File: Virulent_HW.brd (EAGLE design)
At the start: 58.2 x 43 mm, 96 parts, among them SW1 COM08229, SW2 COM08720, SW3 BUTTON, U1 STM32F050G6U6, U2 MAX14536

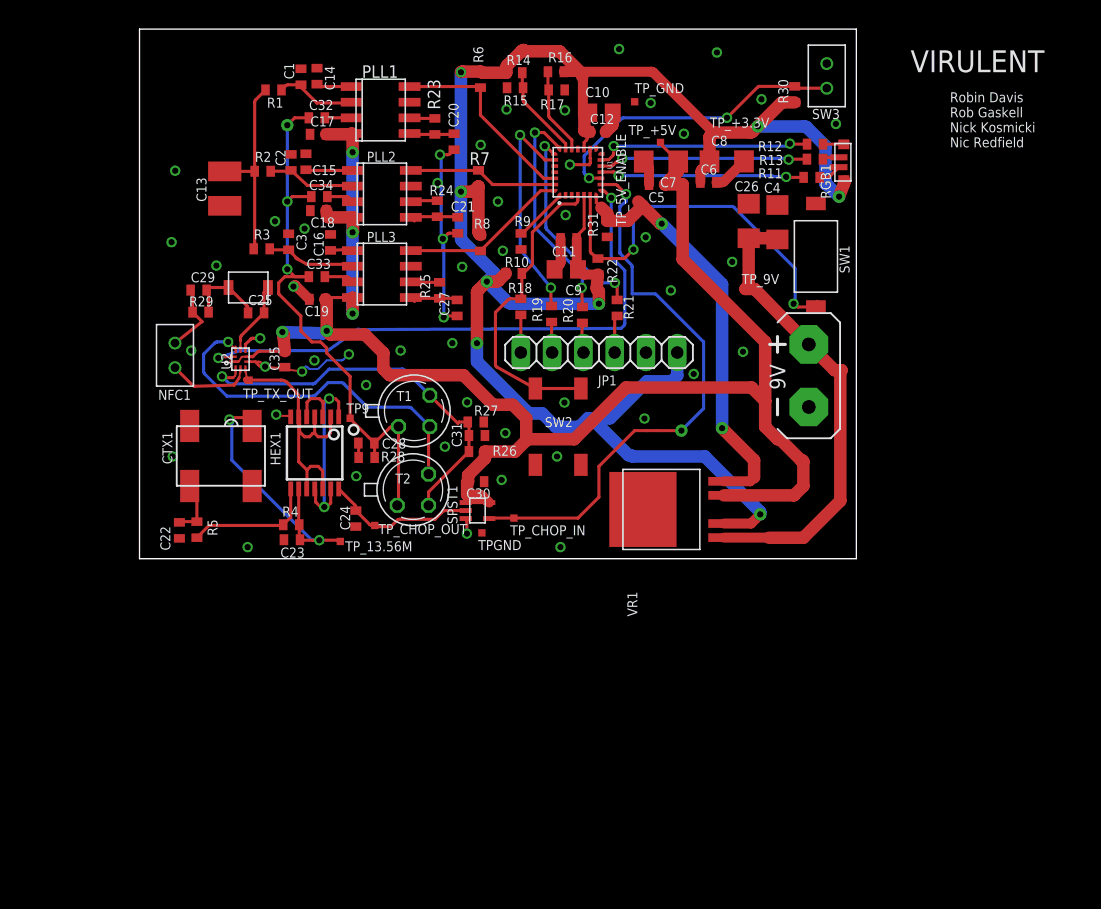
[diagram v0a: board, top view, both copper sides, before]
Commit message: L1 needs to be remade, need SMA conn added to pin 4/pin9 of U2.
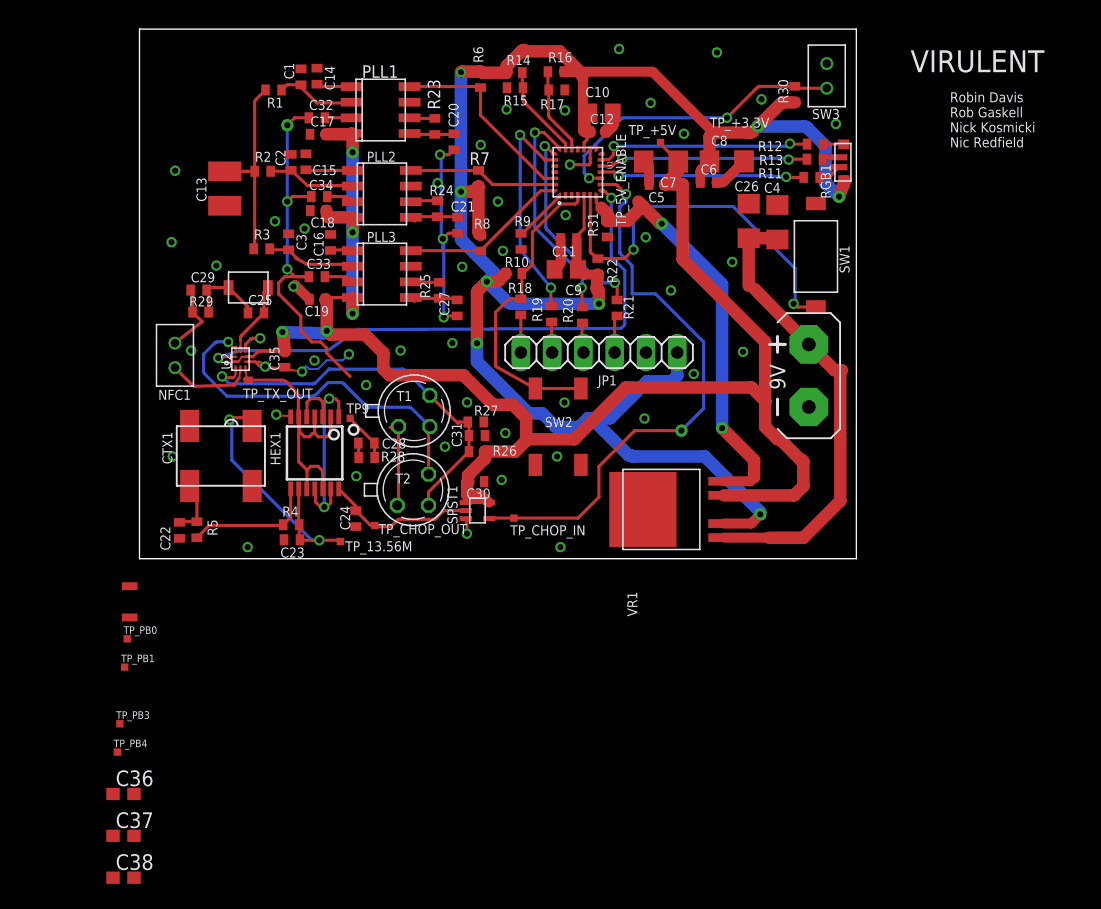
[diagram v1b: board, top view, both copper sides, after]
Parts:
- removed TPGND, TP_9V, TP_GND: TPTP06SQ, testpad:TP06SQ
- added C36, C37, C38: 0.1u, rcl:C0603
- added L1: 100u, Virulent_HW:L1008
- added TP_PB0, TP_PB1, TP_PB3, TP_PB4: TPTP06SQ, testpad:TP06SQ
- C20, C21, C27: value 1n -> 0.1u
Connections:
- removed net N$19: HEX1.8, R4.1, R5.2
- new net N$38: C37.1
- new net N$39: C38.1
- new net N$41: TP_PB4.TP, U1.25
- new net PB0: TP_PB0.TP, U1.14
- new net PB1: TP_PB1.TP, U1.15
- new net PB3: TP_PB3.TP, U1.24
- new net RX_OUT_L: L1.1, T1.1, T2.1
- net +9-36V: no longer TP_9V.TP
- net GND: now also C36.2, C37.2, C38.2; no longer TPGND.TP, TP_GND.TP
- net N$24: now also HEX1.8, R4.1, R5.2
- net N$6: now also C36.1
- net RX_OUT: now also L1.2; no longer T1.1, T2.1
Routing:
- net RX_OUT: track 47.6 -> 35.2 mm
- net N$24: track 19.4 -> 30.0 mm
- net N$19: track 10.6 -> 0.00 mm
- net RX_OUT_L: track 0.00 -> 7.15 mm
- net +9-36V: track 38.5 -> 37.4 mm

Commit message: fixed L1008 part. rearranged board. added SMA connector.
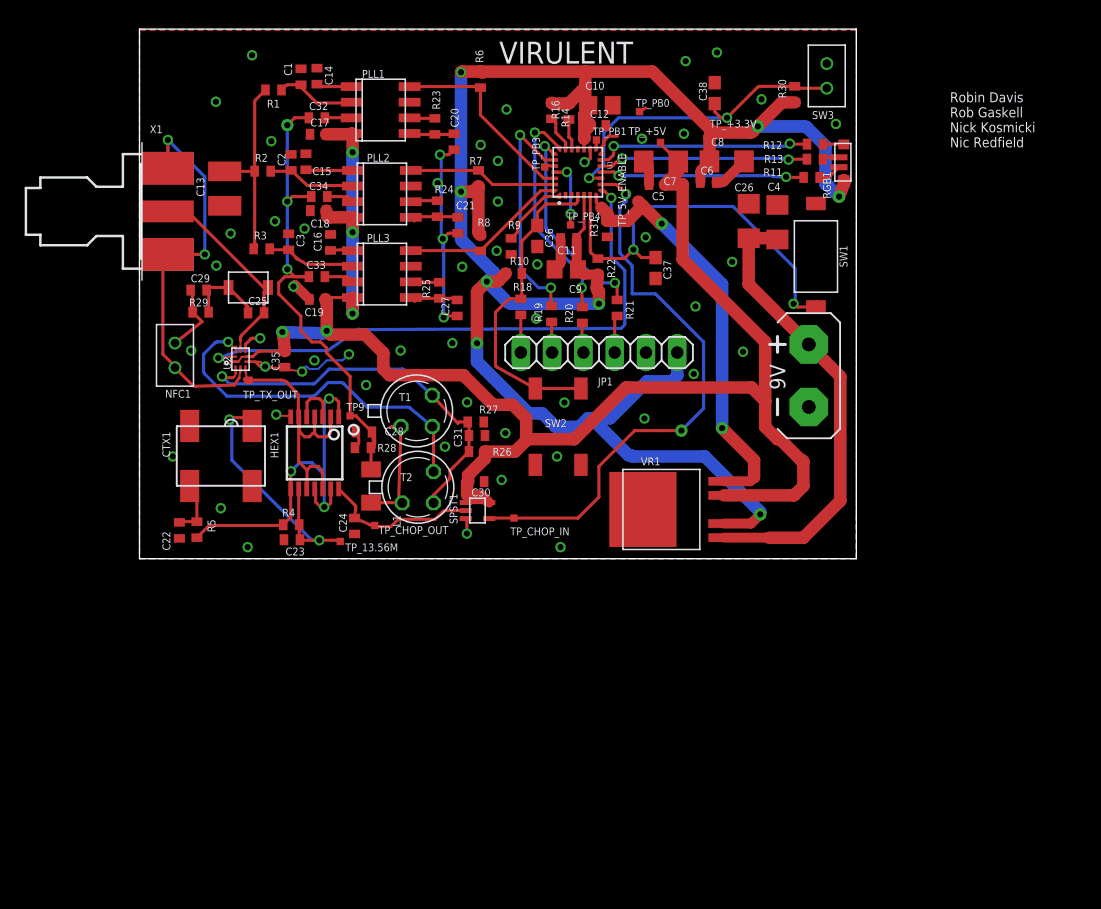
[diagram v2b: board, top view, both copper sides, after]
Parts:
- removed R15, R17: 10k, Virulent_HW:R0402
- added X1: SMA-142-0711-821/826, con-coax:J502-ND-142-0711-821/826
- L1: device Virulent_HW:L1008 -> rcl:L1008
- moved C38 79.8 mm to (46.7, 37.8), turned to 90 degrees
- moved C37 63.2 mm to (41.9, 23.6), turned to 270 degrees
- moved TP_PB0 59.7 mm to (40.6, 36.3)
- moved TP_PB1 57.4 mm to (37.1, 34.0)
- moved TP_PB3 56.9 mm to (32.9, 31.8), turned to 90 degrees
- moved TP_PB4 56.4 mm to (35.0, 27.1)
- moved C36 56.4 mm to (32.3, 26.2), turned to 270 degrees
- moved L1 21.7 mm to (18.8, 5.90), turned to 90 degrees
- moved R14 4.33 mm to (33.5, 36.4), turned to 90 degrees
- moved R16 3.40 mm to (34.9, 36.3), turned to 90 degrees
- moved C28 0.92 mm to (18.2, 10.3)
- moved R9 0.89 mm to (30.2, 25.4)
- moved R28 0.85 mm to (18.1, 9.02)
- moved C24 0.61 mm to (17.5, 2.66)
- moved C10 0.60 mm to (37.5, 36.8)
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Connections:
- removed net N$38: C37.1
- removed net N$39: C38.1
- net GND: no longer R15.1, R17.1
- net N$20: now also X1.1
- net N$32: now also X1.G@1, X1.G@2, X1.G@3, X1.G@4
- net N$34: no longer R17.2
- net NRESET_SOFT: now also C37.1
- net TEAMID1: no longer R15.2
- net TRIGGER: now also C38.1
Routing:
- net N$32: track 6.86 -> 37.8 mm, vias 0 -> 2
- net N$20: track 5.91 -> 16.6 mm
- net RX_OUT: track 35.2 -> 40.8 mm
- net N$41: track 0.00 -> 5.41 mm, vias 0 -> 2
- net N$24: track 30.0 -> 34.8 mm, vias 2 -> 3
- net N$34: track 7.06 -> 2.51 mm
- net TEAMID1: track 7.64 -> 3.39 mm
- net GND: track 50.3 -> 47.2 mm, vias 51 -> 54
- net PB0: track 0.00 -> 2.92 mm
- net RX_OUT_L: track 7.15 -> 10.1 mm
- net NRESET_SOFT: track 31.9 -> 34.0 mm
- net TRIGGER: track 25.0 -> 26.7 mm
- net N$9: track 4.33 -> 5.71 mm
- net PB3: track 0.00 -> 0.86 mm
- net STM_SWO: track 18.4 -> 19.2 mm
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- added copper zone on layer 1, net GND
- added copper zone on layer 16, net GND

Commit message: Added thermal isolation for LDO.
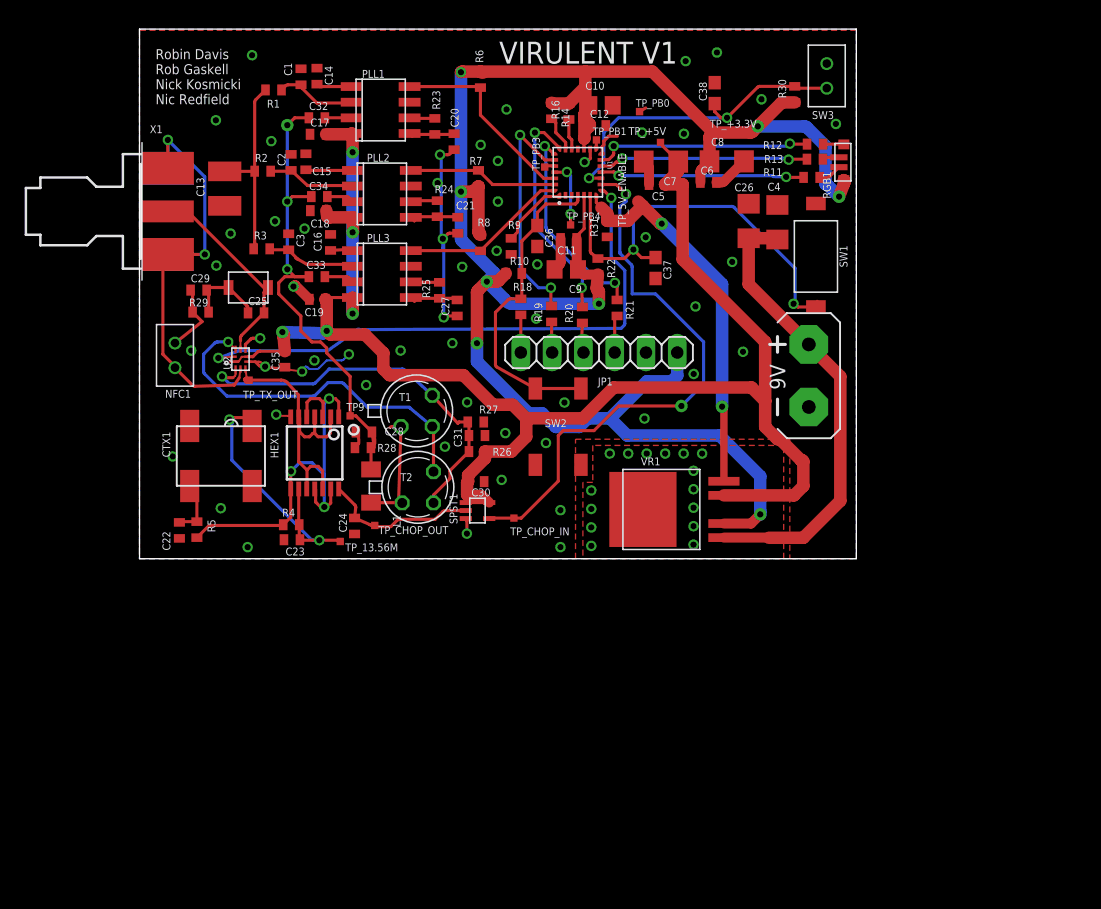
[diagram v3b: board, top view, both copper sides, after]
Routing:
- net 5V_ENABLE: track 34.7 -> 31.4 mm
- net +5V: track 133.5 -> 132.6 mm
- net GND: vias 54 -> 70
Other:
- board text added: "VIRULENT V1"
- board text removed: "VIRULENT"

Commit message: Added mount holes, completed layout.
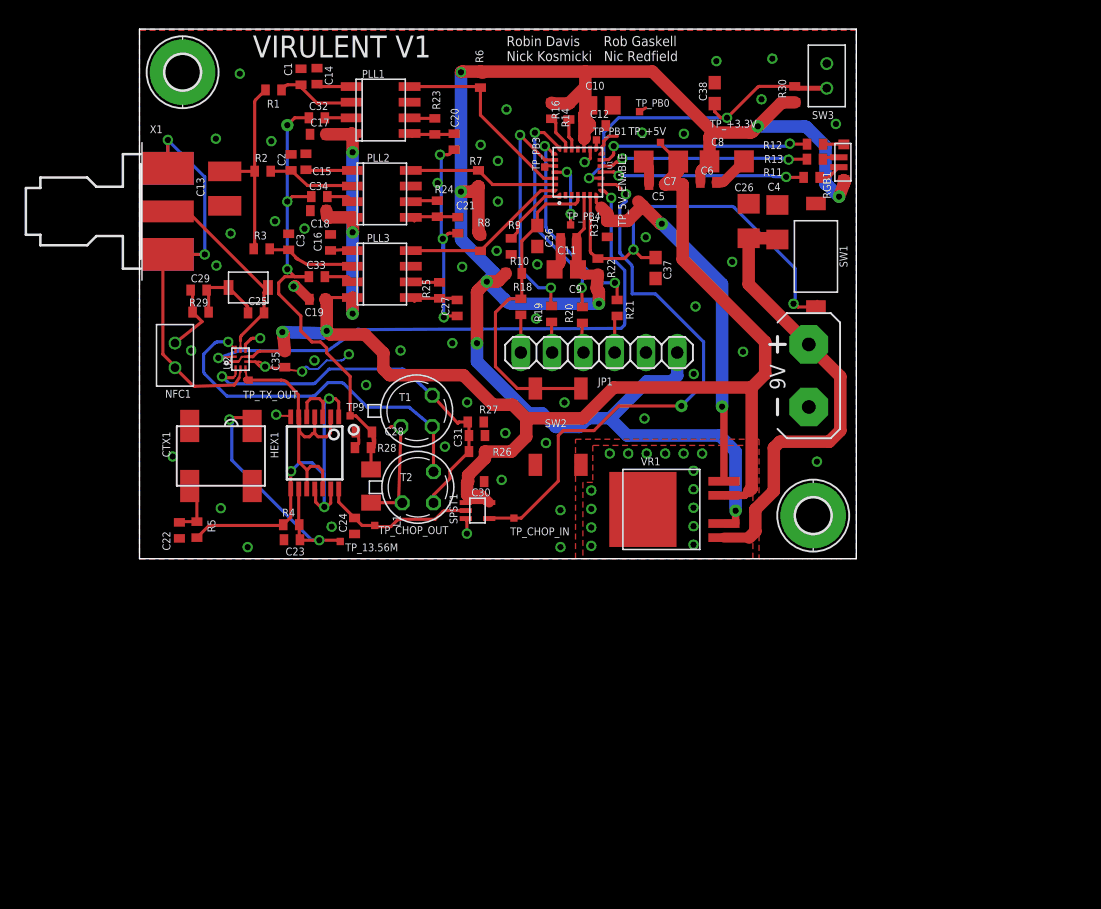
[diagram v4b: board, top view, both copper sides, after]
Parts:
- added H1, H2: MOUNT-PAD-ROUND2.8, holes:2,8-PAD
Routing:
- net +5V: track 132.6 -> 126.0 mm
- net +3.3V: track 158.6 -> 156.0 mm
- net N$6: track 26.0 -> 26.7 mm
- net GND: vias 70 -> 72
